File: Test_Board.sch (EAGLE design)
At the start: 24 parts, among them Q1 MOSFET_PCH-NDS8434, U1 Value, U2 Value

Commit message: initial placements done
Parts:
- removed C3: 0.1UF-0603-100V-10%, SparkFun-Capacitors:0.1UF-0603-100V-10%
- removed D1: 3A/40V/500mV, SparkFun-DiscreteSemi:DIODE-SCHOTTKY-B340A
- added C11: 330uF, brick-capacitor-UCM1H331MNL1GS:UCM1H331MNL1GS
- added J1, J2, J3: (no value), SparkFun-Connectors:CONN_04X2
- added JP1, JP2: JUMPER-SMT_2_NO_NO-SILK, SparkFun-Jumpers:JUMPER-SMT_2_NO_NO-SILK
- added U$4: SWITCHMODE_SCHOTTKY, PowerComponents:SWITCHMODE_SCHOTTKY
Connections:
- new net N$14: JP2.2, Q1.S, RSEN.2
- net +12V: now also C11.+; no longer C3.1
- net +12V_A: now also J1.1, J1.3, J1.5, J1.7
- net +12V_B: now also J2.1, J2.3, J2.5, J2.7
- net +48V: now also J3.1, J3.3, J3.5, J3.7
- net 12V_GND: now also C11.-, J1.2, J1.4, J1.6, J1.8, J2.2, J2.4, J2.6, J2.8; no longer C3.2
- net GND: now also J3.2, J3.4, J3.6, J3.8, U$4.P$1, U$4.P$3; no longer D1.A
- net N$1: now also JP1.2, JP2.1; no longer Q1.S, RSEN.2
- net N$11: now also JP1.1, U$4.P$4; no longer D1.C

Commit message: finished routing, but dont have senior design DRC on my PC to check
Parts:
- removed C6: 100uF, SparkFun-Capacitors:100UF-POLAR-EIA7343-16V-10%(TANT)
- added C3: 150uF, PowerComponents:C-TANTALUM(10UF_150UF)
- added J4: (no value), SparkFun-Connectors:CONN_04X2
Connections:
- removed net 12V_GND: C11.-, J1.2, J1.4, J1.6, J1.8, J2.2, J2.4, J2.6, J2.8
- net +12V: now also J4.1, J4.3, J4.5, J4.7
- net +5V: now also C3.+; no longer C6.+
- net GND: now also C11.-, C3.-, J1.2, J1.4, J1.6, J1.8, J2.2, J2.4, J2.6, J2.8, J4.2, J4.4, J4.6, J4.8; no longer C6.-

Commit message: finished routing. Need DRC
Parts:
- added J5: (no value), SparkFun-Connectors:CONN_041X04_NO_SILK
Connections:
- net +5V: now also J5.3, J5.4
- net GND: now also J5.1, J5.2
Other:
- note added: "12V Input"
- note added: "12V Output"
- note added: "48V Input"
- note added: "5V Output"
- moved on the sheet: J3
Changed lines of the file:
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@@
 <part name="C3" library="PowerComponents" deviceset="C-TANTALUM(10UF_150UF)" device="" value="150uF"/>
 <part name="J4" library="SparkFun-Connectors" library_urn="urn:adsk.eagle:library:513" deviceset="CONN_04X2" device="" package3d_urn="urn:adsk.eagle:package:38103/1"/>
+<part name="J5" library="SparkFun-Connectors" library_urn="urn:adsk.eagle:library:513" deviceset="CONN_04" device="1X04_NO_SILK" package3d_urn="urn:adsk.eagle:package:38094/1"/>
 </parts>
 <sheets>
@@
 <text x="15.24" y="-25.4" size="3.81" layer="91">OR-ing Controller + MOSFETs</text>
 <text x="15.24" y="165.1" size="3.81" layer="91">Buck Controller + Converter</text>
+<text x="20.32" y="104.14" size="1.778" layer="91">48V Input</text>
+<text x="20.32" y="81.28" size="1.778" layer="91">5V Output</text>
+<text x="119.38" y="-20.32" size="1.778" layer="91">12V Input</text>
+<text x="172.72" y="-20.32" size="1.778" layer="91">12V Output</text>
 </plain>
 <instances>
@@
 <attribute name="NAME" x="120.396" y="-42.672" size="1.778" layer="95" font="vector"/>
 </instance>
-<instance part="J3" gate="G$1" x="27.94" y="111.76" smashed="yes">
-<attribute name="VALUE" x="24.13" y="104.394" size="1.778" layer="96" font="vector"/>
-<attribute name="NAME" x="23.876" y="119.888" size="1.778" layer="95" font="vector"/>
+<instance part="J3" gate="G$1" x="33.02" y="91.44" smashed="yes">
+<attribute name="VALUE" x="29.21" y="84.074" size="1.778" layer="96" font="vector"/>
+<attribute name="NAME" x="28.956" y="99.568" size="1.778" layer="95" font="vector"/>
 </instance>
 <instance part="C3" gate="G$1" x="208.28" y="106.68" smashed="yes">
@@
 <attribute name="VALUE" x="173.99" y="-40.386" size="1.778" layer="96" font="vector"/>
 <attribute name="NAME" x="173.736" y="-24.892" size="1.778" layer="95" font="vector"/>
+</instance>
+<instance part="J5" gate="G$1" x="30.48" y="68.58" smashed="yes">
+<attribute name="VALUE" x="25.4" y="61.214" size="1.778" layer="96" font="vector"/>
+<attribute name="NAME" x="25.4" y="76.708" size="1.778" layer="95" font="vector"/>
 </instance>
 </instances>
@@
 <segment>
 <pinref part="J3" gate="G$1" pin="2"/>
-<wire x1="35.56" y1="116.84" x2="38.1" y2="116.84" width="0.1524" layer="91"/>
-<wire x1="38.1" y1="116.84" x2="38.1" y2="114.3" width="0.1524" layer="91"/>
+<wire x1="40.64" y1="96.52" x2="43.18" y2="96.52" width="0.1524" layer="91"/>
+<wire x1="43.18" y1="96.52" x2="43.18" y2="93.98" width="0.1524" layer="91"/>
 <pinref part="J3" gate="G$1" pin="8"/>
-<wire x1="38.1" y1="114.3" x2="38.1" y2="111.76" width="0.1524" layer="91"/>
-<wire x1="38.1" y1="111.76" x2="38.1" y2="109.22" width="0.1524" layer="91"/>
-<wire x1="38.1" y1="109.22" x2="35.56" y2="109.22" width="0.1524" layer="91"/>
+<wire x1="43.18" y1="93.98" x2="43.18" y2="91.44" width="0.1524" layer="91"/>
+<wire x1="43.18" y1="91.44" x2="43.18" y2="88.9" width="0.1524" layer="91"/>
+<wire x1="43.18" y1="88.9" x2="40.64" y2="88.9" width="0.1524" layer="91"/>
 <pinref part="J3" gate="G$1" pin="6"/>
-<wire x1="35.56" y1="111.76" x2="38.1" y2="111.76" width="0.1524" layer="91"/>
-<junction x="38.1" y="111.76"/>
+<wire x1="40.64" y1="91.44" x2="43.18" y2="91.44" width="0.1524" layer="91"/>
+<junction x="43.18" y="91.44"/>
 <pinref part="J3" gate="G$1" pin="4"/>
-<wire x1="35.56" y1="114.3" x2="38.1" y2="114.3" width="0.1524" layer="91"/>
-<junction x="38.1" y="114.3"/>
-<wire x1="38.1" y1="111.76" x2="40.64" y2="111.76" width="0.1524" layer="91"/>
-<label x="40.64" y="111.76" size="1.778" layer="95" xref="yes"/>
+<wire x1="40.64" y1="93.98" x2="43.18" y2="93.98" width="0.1524" layer="91"/>
+<junction x="43.18" y="93.98"/>
+<wire x1="43.18" y1="91.44" x2="45.72" y2="91.44" width="0.1524" layer="91"/>
+<label x="45.72" y="91.44" size="1.778" layer="95" xref="yes"/>
 </segment>
 <segment>
@@
 <wire x1="187.96" y1="-33.02" x2="190.5" y2="-33.02" width="0.1524" layer="91"/>
 <label x="190.5" y="-33.02" size="1.778" layer="95" xref="yes"/>
+</segment>
+<segment>
+<pinref part="J5" gate="G$1" pin="1"/>
+<wire x1="35.56" y1="66.04" x2="38.1" y2="66.04" width="0.1524" layer="91"/>
+<wire x1="38.1" y1="66.04" x2="38.1" y2="68.58" width="0.1524" layer="91"/>
+<pinref part="J5" gate="G$1" pin="2"/>
+<wire x1="38.1" y1="68.58" x2="35.56" y2="68.58" width="0.1524" layer="91"/>
+<wire x1="38.1" y1="66.04" x2="40.64" y2="66.04" width="0.1524" layer="91"/>
+<junction x="38.1" y="66.04"/>
+<label x="40.64" y="66.04" size="1.778" layer="95" xref="yes"/>
 </segment>
 </net>
@@
 <pinref part="L2" gate="G$1" pin="2"/>
 <pinref part="C3" gate="G$1" pin="+"/>
+</segment>
+<segment>
+<pinref part="J5" gate="G$1" pin="3"/>
+<wire x1="35.56" y1="71.12" x2="38.1" y2="71.12" width="0.1524" layer="91"/>
+<wire x1="38.1" y1="71.12" x2="38.1" y2="73.66" width="0.1524" layer="91"/>
+<pinref part="J5" gate="G$1" pin="4"/>
+<wire x1="38.1" y1="73.66" x2="35.56" y2="73.66" width="0.1524" layer="91"/>
+<wire x1="38.1" y1="71.12" x2="40.64" y2="71.12" width="0.1524" layer="91"/>
+<junction x="38.1" y="71.12"/>
+<label x="40.64" y="71.12" size="1.778" layer="95" xref="yes"/>
 </segment>
 </net>
@@
 <segment>
 <pinref part="J3" gate="G$1" pin="1"/>
-<wire x1="20.32" y1="116.84" x2="17.78" y2="116.84" width="0.1524" layer="91"/>
-<wire x1="17.78" y1="116.84" x2="17.78" y2="114.3" width="0.1524" layer="91"/>
+<wire x1="25.4" y1="96.52" x2="22.86" y2="96.52" width="0.1524" layer="91"/>
+<wire x1="22.86" y1="96.52" x2="22.86" y2="93.98" width="0.1524" layer="91"/>
 <pinref part="J3" gate="G$1" pin="7"/>
-<wire x1="17.78" y1="114.3" x2="17.78" y2="111.76" width="0.1524" layer="91"/>
-<wire x1="17.78" y1="111.76" x2="17.78" y2="109.22" width="0.1524" layer="91"/>
-<wire x1="17.78" y1="109.22" x2="20.32" y2="109.22" width="0.1524" layer="91"/>
+<wire x1="22.86" y1="93.98" x2="22.86" y2="91.44" width="0.1524" layer="91"/>
+<wire x1="22.86" y1="91.44" x2="22.86" y2="88.9" width="0.1524" layer="91"/>
+<wire x1="22.86" y1="88.9" x2="25.4" y2="88.9" width="0.1524" layer="91"/>
 <pinref part="J3" gate="G$1" pin="5"/>
-<wire x1="20.32" y1="111.76" x2="17.78" y2="111.76" width="0.1524" layer="91"/>
-<junction x="17.78" y="111.76"/>
+<wire x1="25.4" y1="91.44" x2="22.86" y2="91.44" width="0.1524" layer="91"/>
+<junction x="22.86" y="91.44"/>
 <pinref part="J3" gate="G$1" pin="3"/>
-<wire x1="20.32" y1="114.3" x2="17.78" y2="114.3" width="0.1524" layer="91"/>
-<junction x="17.78" y="114.3"/>
-<wire x1="17.78" y1="111.76" x2="15.24" y2="111.76" width="0.1524" layer="91"/>
-<label x="15.24" y="111.76" size="1.778" layer="95" rot="R180" xref="yes"/>
-</segment>
-</net>
+<wire x1="25.4" y1="93.98" x2="22.86" y2="93.98" width="0.1524" layer="91"/>
+<junction x="22.86" y="93.98"/>
+<wire x1="22.86" y1="91.44" x2="20.32" y2="91.44" width="0.1524" layer="91"/>
+<label x="20.32" y="91.44" size="1.778" layer="95" rot="R180" xref="yes"/>
+</segment>
+</net>

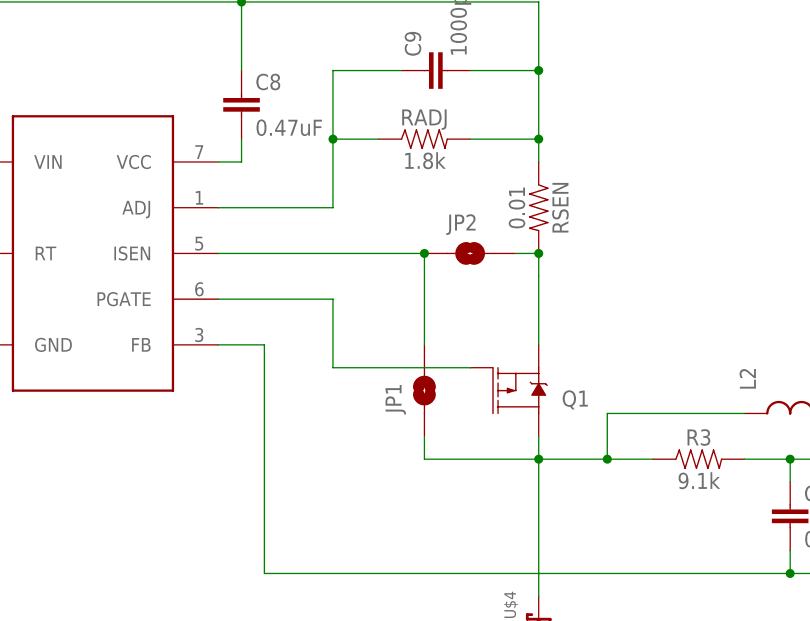
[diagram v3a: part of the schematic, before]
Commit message: added sense resistor
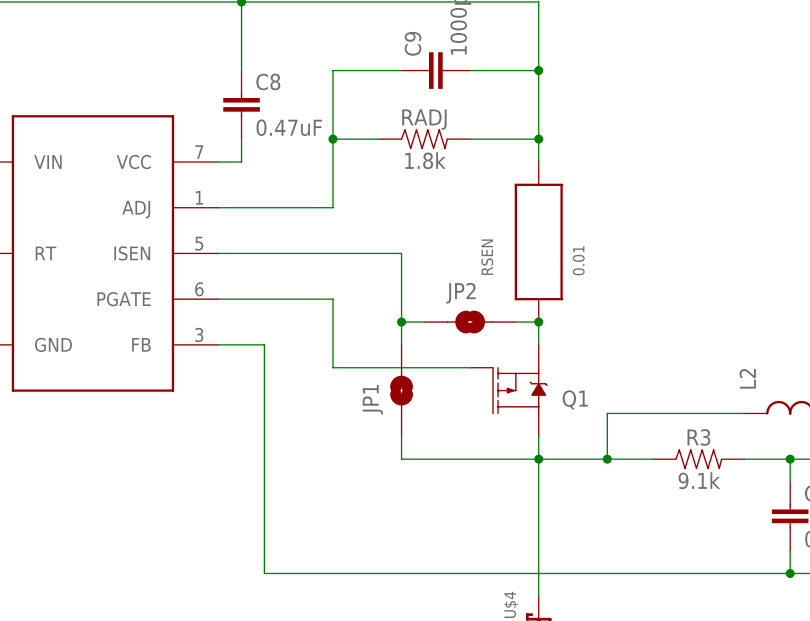
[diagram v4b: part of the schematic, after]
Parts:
- RSEN: device SparkFun-Resistors:RESISTOR0603 -> INA4181A4:CSS2H-2512
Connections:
- net N$1 renamed ISEN
- net +48V: now also RSEN.2; no longer RSEN.1
- net N$14: now also RSEN.1; no longer RSEN.2
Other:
- moved on the sheet: JP1, JP2
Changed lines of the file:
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@@
 <part name="RADJ" library="SparkFun-Resistors" library_urn="urn:adsk.eagle:library:532" deviceset="RESISTOR" device="0603" package3d_urn="urn:adsk.eagle:package:39650/1" value="1.8k"/>
 <part name="RFB2" library="SparkFun-Resistors" library_urn="urn:adsk.eagle:library:532" deviceset="RESISTOR" device="0603" package3d_urn="urn:adsk.eagle:package:39650/1" value="10k"/>
-<part name="RSEN" library="SparkFun-Resistors" library_urn="urn:adsk.eagle:library:532" deviceset="RESISTOR" device="0603" package3d_urn="urn:adsk.eagle:package:39650/1" value="0.01"/>
 <part name="R3" library="SparkFun-Resistors" library_urn="urn:adsk.eagle:library:532" deviceset="RESISTOR" device="0603" package3d_urn="urn:adsk.eagle:package:39650/1" value="9.1k"/>
 <part name="C7" library="brick-capacitor-UCM1H331MNL1GS" deviceset="UCM1H331MNL1GS" device="" package3d_urn="urn:adsk.eagle:package:24202090/2" value="47uF"/>
@@
 <part name="J4" library="SparkFun-Connectors" library_urn="urn:adsk.eagle:library:513" deviceset="CONN_04X2" device="" package3d_urn="urn:adsk.eagle:package:38103/1"/>
 <part name="J5" library="SparkFun-Connectors" library_urn="urn:adsk.eagle:library:513" deviceset="CONN_04" device="1X04_NO_SILK" package3d_urn="urn:adsk.eagle:package:38094/1"/>
+<part name="RSEN" library="INA4181A4" deviceset="CSS2H-2512" device="" value="0.01"/>
 </parts>
 <sheets>
@@
 <attribute name="VALUE" x="194.056" y="109.22" size="1.778" layer="96" font="vector" rot="R270" align="top-center"/>
 </instance>
-<instance part="RSEN" gate="G$1" x="139.7" y="139.7" smashed="yes" rot="R270">
-<attribute name="NAME" x="141.224" y="139.7" size="1.778" layer="95" font="vector" rot="R270" align="bottom-center"/>
-<attribute name="VALUE" x="138.176" y="139.7" size="1.778" layer="96" font="vector" rot="R270" align="top-center"/>
-</instance>
 <instance part="R3" gate="G$1" x="157.48" y="111.76" smashed="yes">
 <attribute name="NAME" x="157.48" y="113.284" size="1.778" layer="95" font="vector" align="bottom-center"/>
@@
 <attribute name="VALUE" x="176.53" y="119.38" size="1.778" layer="96" rot="R90"/>
 </instance>
-<instance part="JP1" gate="G$1" x="127" y="119.38" smashed="yes" rot="R90">
-<attribute name="NAME" x="124.46" y="116.84" size="1.778" layer="95" font="vector" rot="R90"/>
-</instance>
-<instance part="JP2" gate="G$1" x="132.08" y="134.62" smashed="yes">
-<attribute name="NAME" x="129.54" y="137.16" size="1.778" layer="95" font="vector"/>
+<instance part="JP1" gate="G$1" x="124.46" y="119.38" smashed="yes" rot="R90">
+<attribute name="NAME" x="121.92" y="116.84" size="1.778" layer="95" font="vector" rot="R90"/>
+</instance>
+<instance part="JP2" gate="G$1" x="132.08" y="127" smashed="yes">
+<attribute name="NAME" x="129.54" y="129.54" size="1.778" layer="95" font="vector"/>
 </instance>
 <instance part="U$4" gate="G$1" x="139.7" y="93.98" smashed="yes" rot="R90">
@@
 <attribute name="VALUE" x="25.4" y="61.214" size="1.778" layer="96" font="vector"/>
 <attribute name="NAME" x="25.4" y="76.708" size="1.778" layer="95" font="vector"/>
+</instance>
+<instance part="RSEN" gate="G$1" x="139.7" y="134.62" smashed="yes" rot="R90">
+<attribute name="NAME" x="134.62" y="132.08" size="1.27" layer="95" rot="R90"/>
+<attribute name="VALUE" x="144.78" y="132.08" size="1.27" layer="96" rot="R90"/>
 </instance>
 </instances>
@@
 <wire x1="139.7" y1="147.32" x2="139.7" y2="154.94" width="0.1524" layer="91"/>
 <junction x="139.7" y="154.94"/>
-<pinref part="RSEN" gate="G$1" pin="1"/>
 <wire x1="139.7" y1="147.32" x2="139.7" y2="144.78" width="0.1524" layer="91"/>
 <junction x="139.7" y="147.32"/>
@@
 <pinref part="C9" gate="G$1" pin="2"/>
 <pinref part="C4" gate="G$1" pin="1"/>
+<pinref part="RSEN" gate="G$1" pin="2"/>
 </segment>
 <segment>
@@
 <pinref part="L2" gate="G$1" pin="1"/>
 <pinref part="JP1" gate="G$1" pin="1"/>
-<wire x1="127" y1="114.3" x2="127" y2="111.76" width="0.1524" layer="91"/>
-<wire x1="127" y1="111.76" x2="139.7" y2="111.76" width="0.1524" layer="91"/>
+<wire x1="124.46" y1="114.3" x2="124.46" y2="111.76" width="0.1524" layer="91"/>
+<wire x1="124.46" y1="111.76" x2="139.7" y2="111.76" width="0.1524" layer="91"/>
 <pinref part="U$4" gate="G$1" pin="P$4"/>
 </segment>
@@
 </segment>
 </net>
-<net name="N$1" class="0">
+<net name="ISEN" class="0">
 <segment>
 <pinref part="U$3" gate="G$1" pin="ISEN"/>
-<wire x1="104.14" y1="134.62" x2="127" y2="134.62" width="0.1524" layer="91"/>
+<wire x1="104.14" y1="134.62" x2="124.46" y2="134.62" width="0.1524" layer="91"/>
+<wire x1="124.46" y1="134.62" x2="124.46" y2="127" width="0.1524" layer="91"/>
+<wire x1="124.46" y1="127" x2="127" y2="127" width="0.1524" layer="91"/>
+<pinref part="JP2" gate="G$1" pin="1"/>
 <pinref part="JP1" gate="G$1" pin="2"/>
-<wire x1="127" y1="124.46" x2="127" y2="134.62" width="0.1524" layer="91"/>
-<pinref part="JP2" gate="G$1" pin="1"/>
-<junction x="127" y="134.62"/>
+<wire x1="124.46" y1="124.46" x2="124.46" y2="127" width="0.1524" layer="91"/>
+<junction x="124.46" y="127"/>
 </segment>
 </net>
@@
 <segment>
 <pinref part="JP2" gate="G$1" pin="2"/>
-<pinref part="RSEN" gate="G$1" pin="2"/>
-<wire x1="137.16" y1="134.62" x2="139.7" y2="134.62" width="0.1524" layer="91"/>
+<wire x1="137.16" y1="127" x2="139.7" y2="127" width="0.1524" layer="91"/>
 <pinref part="Q1" gate="G$1" pin="S"/>
-<wire x1="139.7" y1="134.104740625" x2="139.7" y2="132.08" width="0.1524" layer="91"/>
-<wire x1="139.7" y1="132.08" x2="139.7" y2="124.46" width="0.1524" layer="91"/>
-<wire x1="139.7" y1="134.62" x2="139.7" y2="134.104740625" width="0.1524" layer="91"/>
-<junction x="139.7" y="134.62"/>
-</segment>
-</net>
+<wire x1="139.7" y1="127" x2="139.7" y2="124.46" width="0.1524" layer="91"/>
+<pinref part="RSEN" gate="G$1" pin="1"/>
+<junction x="139.7" y="127"/>
+</segment>
+</net>

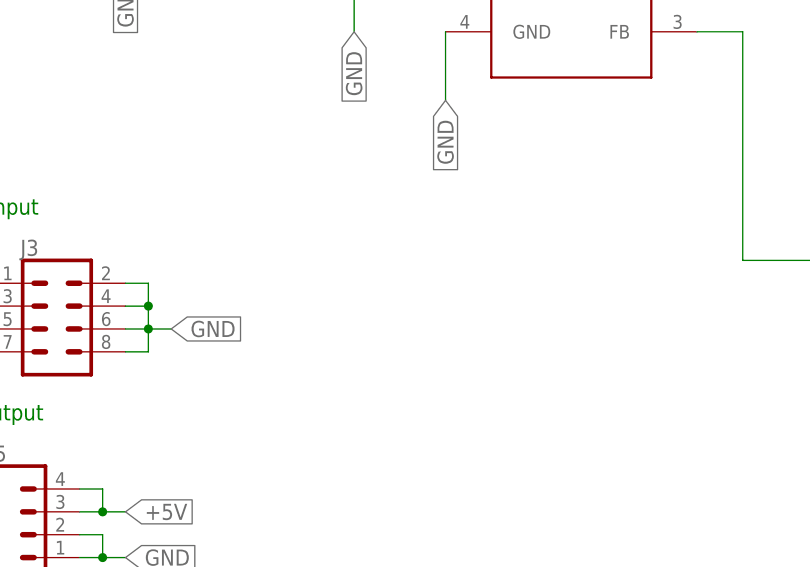
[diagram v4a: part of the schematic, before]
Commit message: rerouted buck converter, trying to mitigate distance and also follow the recommended layout
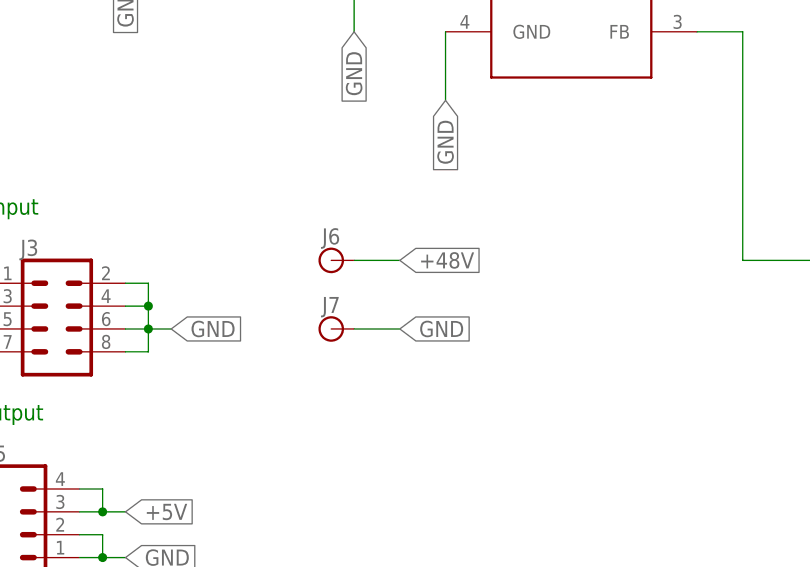
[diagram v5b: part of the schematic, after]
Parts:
- added J6, J7: (no value), SparkFun-Connectors:BANANA_CONN
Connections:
- net N$15 renamed RT
- net N$16 renamed FB
- net N$3 renamed VCC
- net N$4 renamed GATE
- net +48V: now also J6.1
- net GND: now also J7.1
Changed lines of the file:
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@@
 <part name="J5" library="SparkFun-Connectors" library_urn="urn:adsk.eagle:library:513" deviceset="CONN_04" device="1X04_NO_SILK" package3d_urn="urn:adsk.eagle:package:38094/1"/>
 <part name="RSEN" library="INA4181A4" deviceset="CSS2H-2512" device="" value="0.01"/>
+<part name="J6" library="SparkFun-Connectors" library_urn="urn:adsk.eagle:library:513" deviceset="BANANA_CONN" device="" package3d_urn="urn:adsk.eagle:package:38018/1"/>
+<part name="J7" library="SparkFun-Connectors" library_urn="urn:adsk.eagle:library:513" deviceset="BANANA_CONN" device="" package3d_urn="urn:adsk.eagle:package:38018/1"/>
 </parts>
 <sheets>
@@
 <attribute name="NAME" x="134.62" y="132.08" size="1.27" layer="95" rot="R90"/>
 <attribute name="VALUE" x="144.78" y="132.08" size="1.27" layer="96" rot="R90"/>
+</instance>
+<instance part="J6" gate="G$1" x="63.5" y="99.06" smashed="yes" rot="MR0">
+<attribute name="NAME" x="64.516" y="100.838" size="1.778" layer="95" font="vector" rot="MR0"/>
+<attribute name="VALUE" x="64.516" y="96.012" size="1.778" layer="96" font="vector" rot="MR0"/>
+</instance>
+<instance part="J7" gate="G$1" x="63.5" y="91.44" smashed="yes" rot="MR0">
+<attribute name="NAME" x="64.516" y="93.218" size="1.778" layer="95" font="vector" rot="MR0"/>
+<attribute name="VALUE" x="64.516" y="88.392" size="1.778" layer="96" font="vector" rot="MR0"/>
 </instance>
 </instances>
@@
 <junction x="38.1" y="66.04"/>
 <label x="40.64" y="66.04" size="1.778" layer="95" xref="yes"/>
+</segment>
+<segment>
+<pinref part="J7" gate="G$1" pin="1"/>
+<wire x1="66.04" y1="91.44" x2="71.12" y2="91.44" width="0.1524" layer="91"/>
+<label x="71.12" y="91.44" size="1.778" layer="95" xref="yes"/>
 </segment>
 </net>
@@
 <label x="20.32" y="91.44" size="1.778" layer="95" rot="R180" xref="yes"/>
 </segment>
-</net>
-<net name="N$3" class="0">
+<segment>
+<pinref part="J6" gate="G$1" pin="1"/>
+<wire x1="66.04" y1="99.06" x2="71.12" y2="99.06" width="0.1524" layer="91"/>
+<label x="71.12" y="99.06" size="1.778" layer="95" xref="yes"/>
+</segment>
+</net>
+<net name="VCC" class="0">
 <segment>
 <pinref part="U$3" gate="G$1" pin="VCC"/>
@@
 </segment>
 </net>
-<net name="N$4" class="0">
+<net name="GATE" class="0">
 <segment>
 <pinref part="U$3" gate="G$1" pin="PGATE"/>
@@
 </segment>
 </net>
-<net name="N$15" class="0">
+<net name="RT" class="0">
 <segment>
 <pinref part="RT" gate="G$1" pin="1"/>
@@
 </segment>
 </net>
-<net name="N$16" class="0">
+<net name="FB" class="0">
 <segment>
 <pinref part="U$3" gate="G$1" pin="FB"/>

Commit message: bigger U and a few labels. inductor pour cutout
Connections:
- net N$11 renamed SW
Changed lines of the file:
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@@
 <?xml version="1.0" encoding="utf-8"?>
 <!DOCTYPE eagle SYSTEM "eagle.dtd">
-<eagle version="9.5.0">
+<eagle version="9.6.0">
 <drawing>
 <settings>
@@
 </segment>
 </net>
-<net name="N$11" class="0">
+<net name="SW" class="0">
 <segment>
 <pinref part="Q1" gate="G$1" pin="D"/>
